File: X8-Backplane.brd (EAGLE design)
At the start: 122.1 x 106.6 mm, 17 parts, among them IC1 MAX3467CPA, U1 LM2678

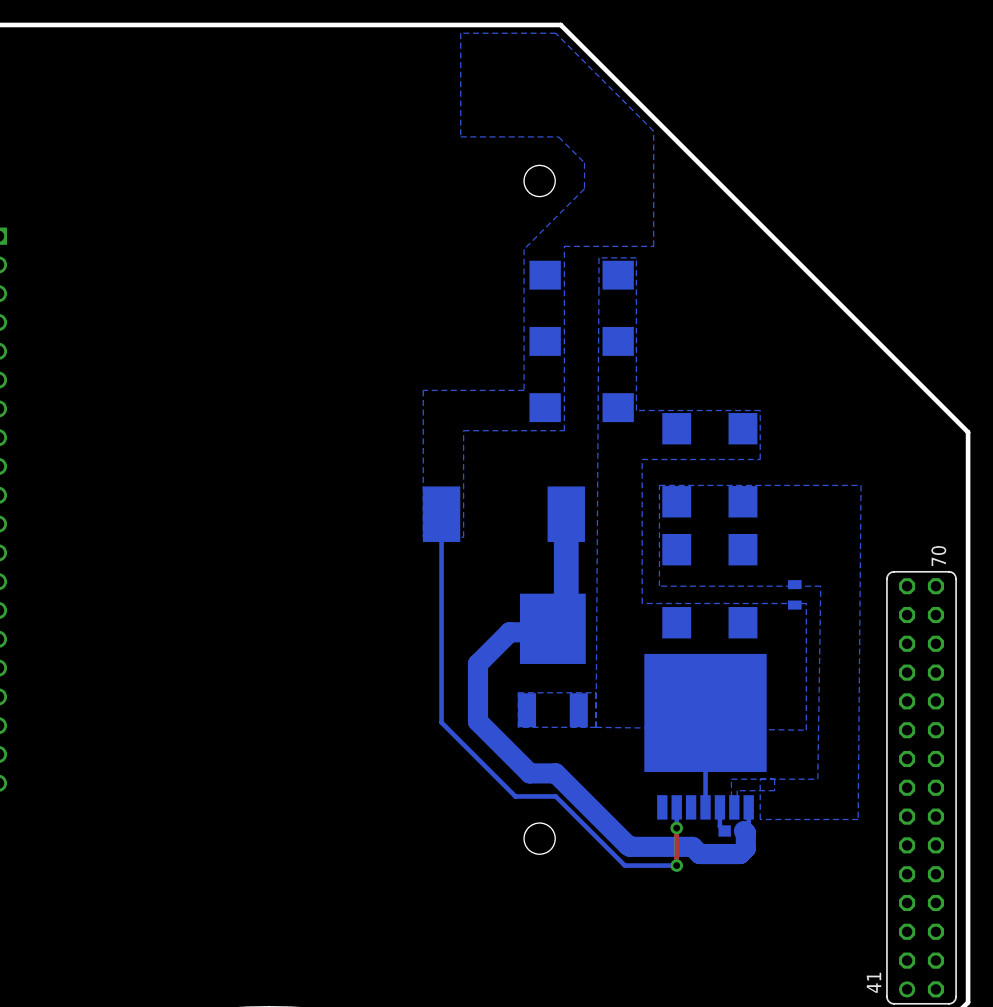
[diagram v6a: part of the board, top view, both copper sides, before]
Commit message: Mostly routed
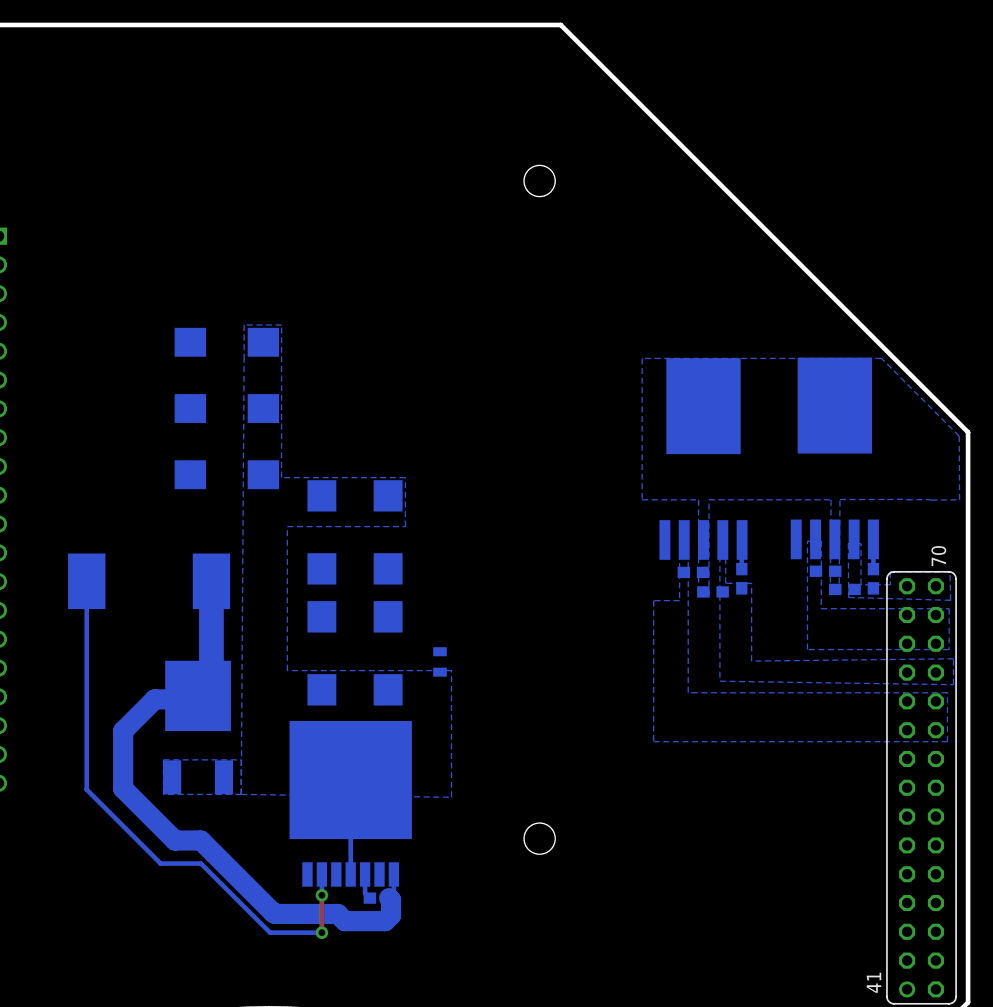
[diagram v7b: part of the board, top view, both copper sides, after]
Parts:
- added C1, C7: 10uF, SparkFun-Passives:0603-CAP
- added C5, C8: 0.1uF, SparkFun-Passives:0603-CAP
- added R1, R2: 10k, SparkFun-Passives:0603-RES
- added U2, U3: MIC29501-5.0WU, LDO:TO-263-5
- moved C10 31.8 mm to (59.1, 65.5)
- moved C6 31.8 mm to (59.1, 71.3)
- moved C9 31.8 mm to (59.1, 59.6)
- moved C11 31.8 mm to (67.5, 43.9)
- moved C12 31.8 mm to (67.5, 54.5)
- moved C13 31.8 mm to (73.4, 43.9)
- moved C2 31.8 mm to (73.4, 54.5)
- moved C3 31.8 mm to (77.9, 43.1)
- moved C4 31.8 mm to (72.6, 22.3)
- moved U$1 31.8 mm to (56.6, 37.0)
- moved U$2 31.8 mm to (52.3, 50.2)
- moved U1 31.8 mm to (70.1, 32.7)
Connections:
- new net +5V_CAMERA: C7.1, U$4.65, U$4.66, U$4.67, U$4.68, U3.4
- new net EN1: R1.1, U2.1
- new net EN2: R2.1, U3.1
- net +12V: now also C5.1, C8.1, R1.2, R2.2, U$4.63, U$4.64, U$4.69, U$4.70, U2.2, U3.2
- net +5V: now also C1.1, U$4.59, U$4.60, U$4.61, U$4.62, U2.4
- net GND: now also C1.2, C5.2, C7.2, C8.2, U2.3, U2.6, U3.3, U3.6
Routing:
- net EN2: track 0.00 -> 2.62 mm
- net EN1: track 0.00 -> 2.59 mm
- added copper zone on layer 16, net +5V_CAMERA

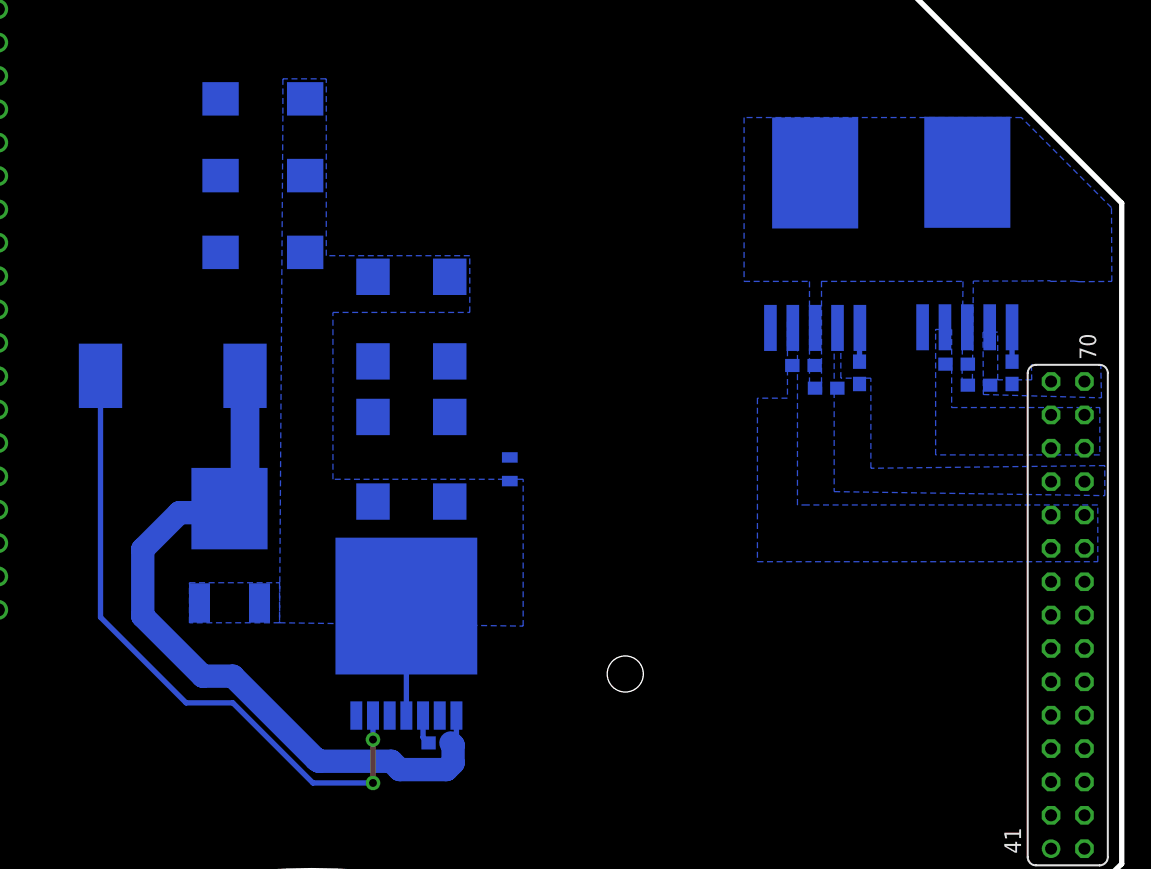
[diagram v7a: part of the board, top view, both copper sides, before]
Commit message: removed buck regulator circuit
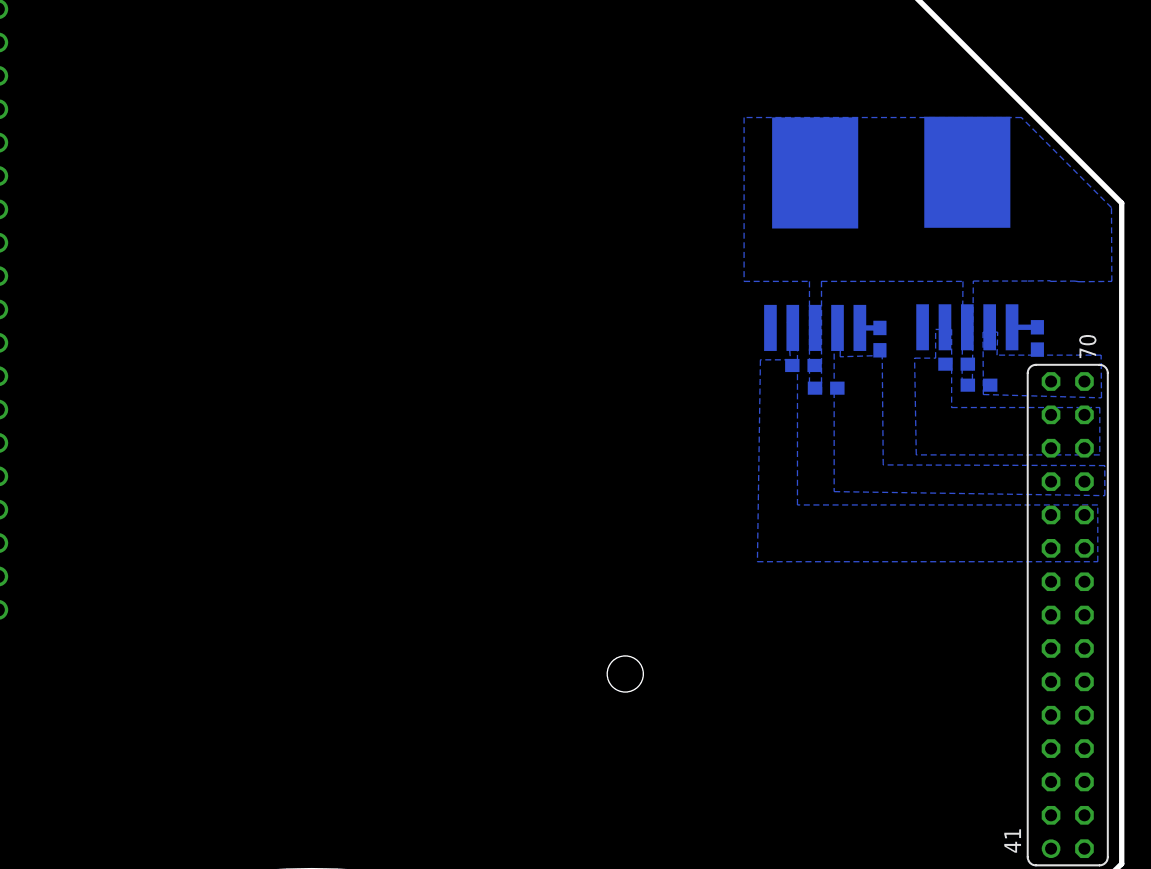
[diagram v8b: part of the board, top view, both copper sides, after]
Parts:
- removed C10, C6, C9: 150uF, PowerComponents:CTAN(7.30_4.30MM)
- removed C11, C12, C13, C2: 10uF, PowerComponents:CTAN(7.30_4.30MM)
- removed C3: 0.47uF, SparkFun-Capacitors:0805
- removed C4: 0.01uF, SparkFun-Passives:0603-CAP
- removed U$1: SWITCHMODE_SCHOTTKY, PowerComponents:DPAK-3
- removed U$2: 15uH, DiscreteComponents:HCMA1305
- removed U1: LM2678, PowerComponents:LM2678
- moved R2 3.25 mm to (118.1, 53.1)
- moved R1 3.00 mm to (106.1, 53.0)
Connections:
- net +5V_CAMERA renamed +5V_CAMERA_TUBE
- removed net N$2: C4.1, U1.3
- removed net N$3: C4.2, U$1.P$4, U$2.P$1, U1.1
- net +12V: no longer C11.+, C12.+, C13.+, C2.+, C3.1, U1.2
- net +5V: no longer C10.+, C6.+, C9.+, U$2.P$2, U1.6
- net GND: no longer C10.-, C11.-, C12.-, C13.-, C2.-, C3.2, C6.-, C9.-, U$1.P$1, U$1.P$3, U1.4, U1.TAB
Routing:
- net N$3: track 56.7 -> 0.00 mm
- net +5V: track 49.5 -> 0.00 mm, vias 2 -> 0
- net GND: track 8.33 -> 0.00 mm
- net N$2: track 2.26 -> 0.00 mm
- net EN1: track 2.59 -> 1.55 mm
- net EN2: track 2.62 -> 1.93 mm
